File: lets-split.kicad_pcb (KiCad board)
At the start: 2 copper layers, 124 x 85.9 mm, 60 parts, among them J1 USB_C_Receptacle_USB2.0, SW1 Key_Tab, SW10 Key_D, SW11 Key_F, SW12 Key_G, SW13 Key_Shift, SW14 Key_Z, SW15 Key_X, SW16 Key_C, SW17 Key_V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

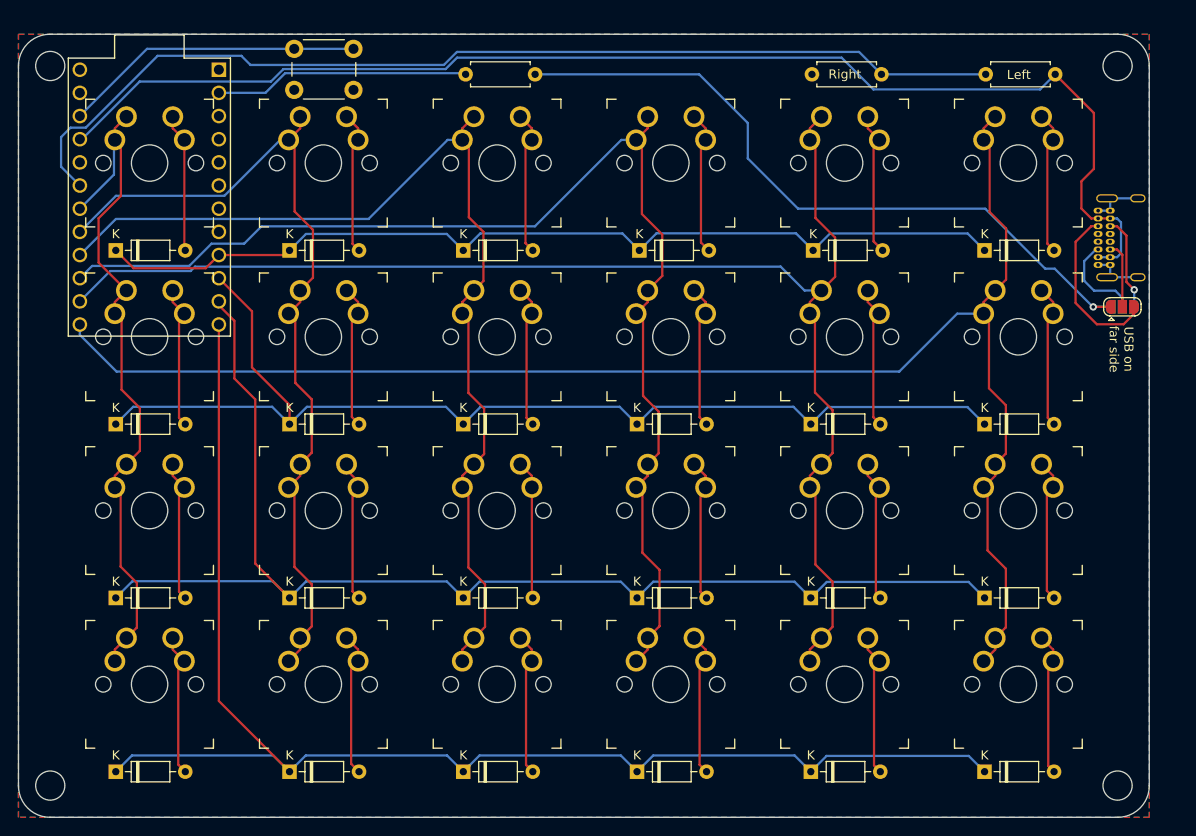
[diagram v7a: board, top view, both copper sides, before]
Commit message: Reversed column pin order to tidy PCB
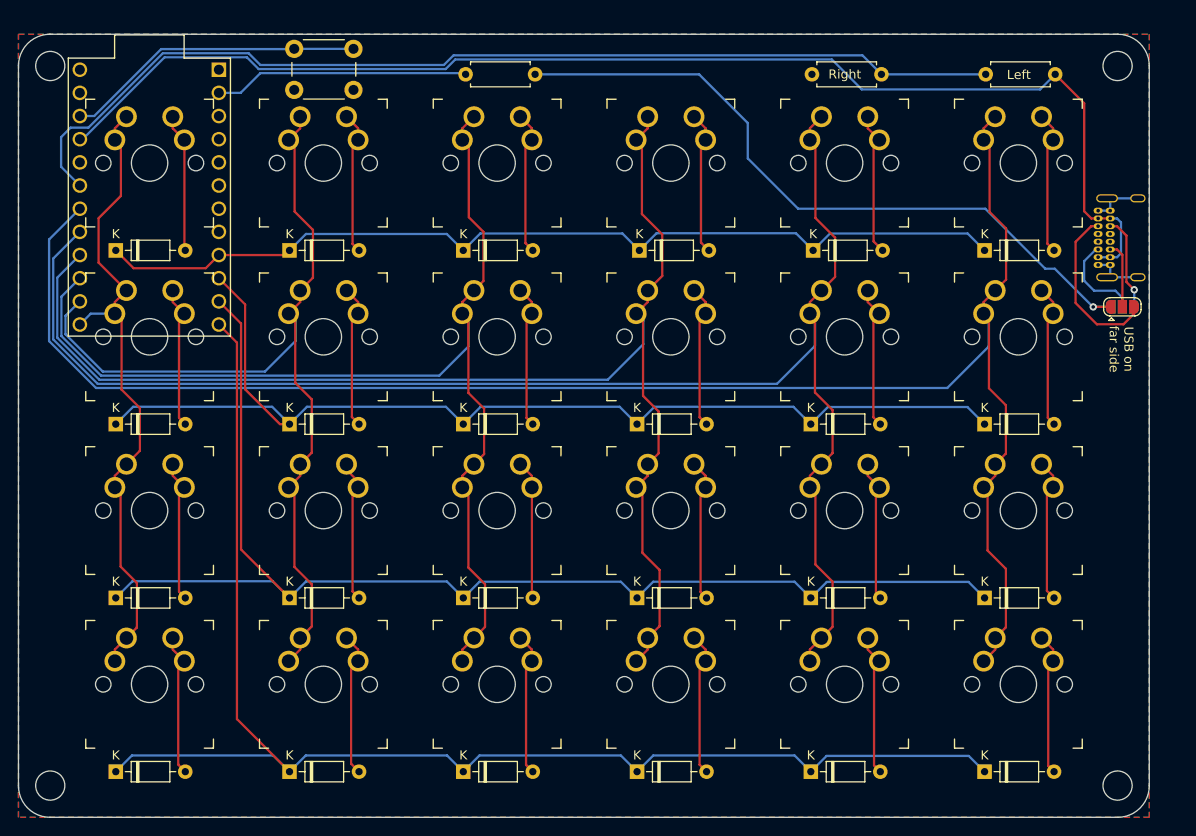
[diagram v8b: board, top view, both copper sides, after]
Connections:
- U1 pad 13: Col6 -> Col1
- U1 pad 14: Col5 -> Col2
- U1 pad 15: Col4 -> Col3
- U1 pad 16: Col3 -> Col4
- U1 pad 17: Col2 -> Col5
- U1 pad 18: Col1 -> Col6
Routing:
- net Col6: track 170.8 -> 193.1 mm
- net Col5: track 150.6 -> 170.7 mm
- net Col4: track 134.0 -> 148.3 mm
- net Col3: track 113.3 -> 125.0 mm
- net Col2: track 93.7 -> 103.4 mm
- net Col1: track 76.7 -> 72.0 mm
- net Row2: track 122.3 -> 122.9 mm
